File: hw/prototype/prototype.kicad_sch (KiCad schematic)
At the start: 0 parts

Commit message: More KiCAD files
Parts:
- added C1: C, symbol Device:C
- added D1: LED, LED_SMD:LED_Cree-XHP50_3V_HighDensity, symbol Device:LED
- added D2: D_Photo, OptoDevice:Kodenshi_LG206D, symbol Device:D_Photo
- added R1, R2: R_US, symbol Device:R_US
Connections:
- new net: D1.2 (A), R1.2
- new net GND: D1.1 (K), D2.2 (A)
- new net VCC: R1.1

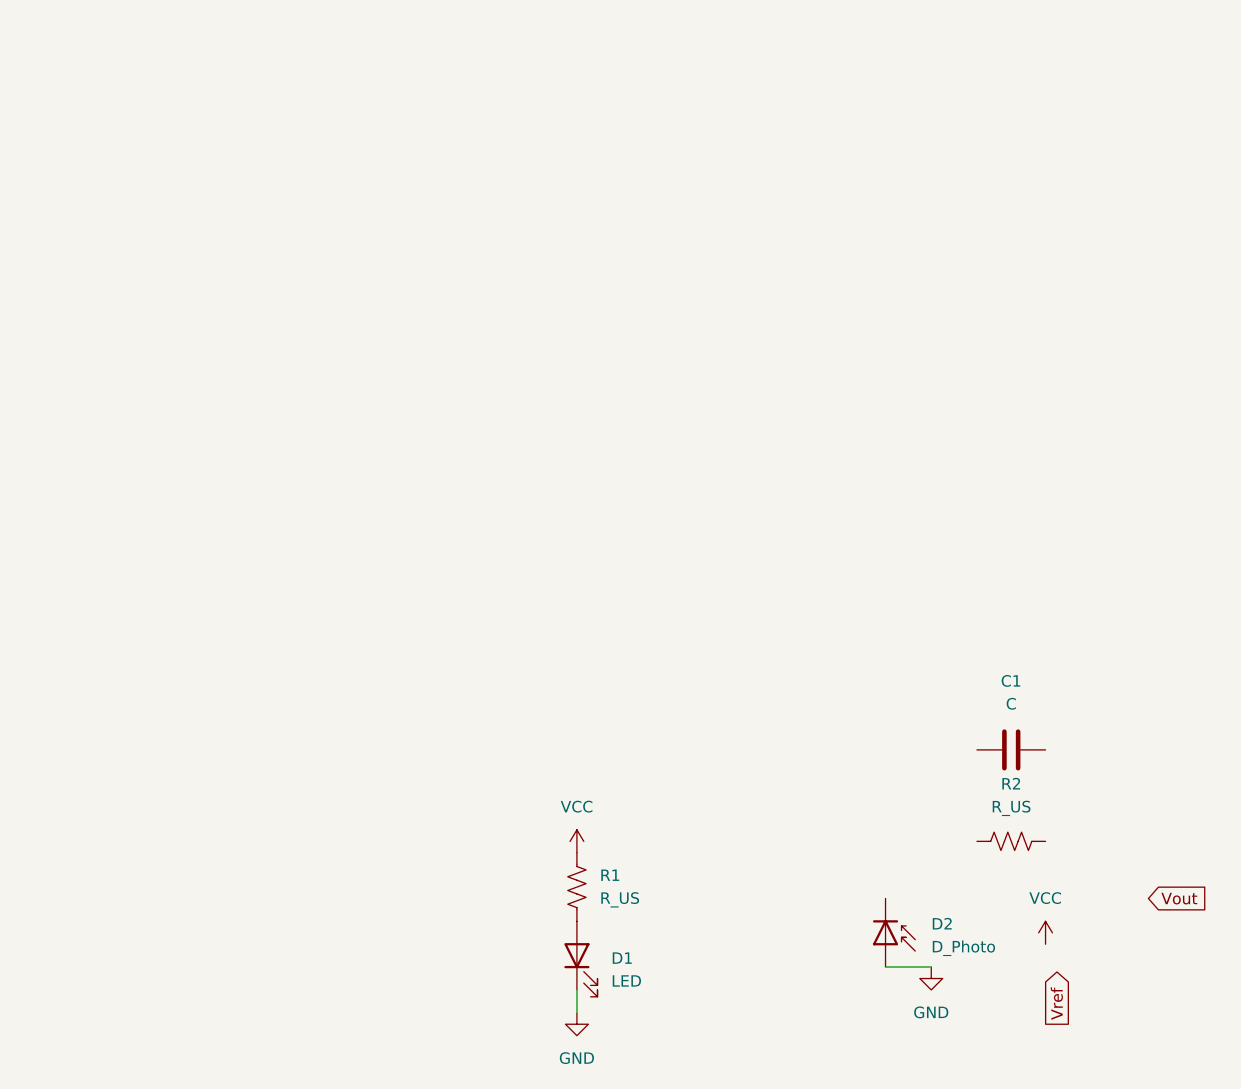
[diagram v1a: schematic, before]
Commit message: Added modified TI reference design
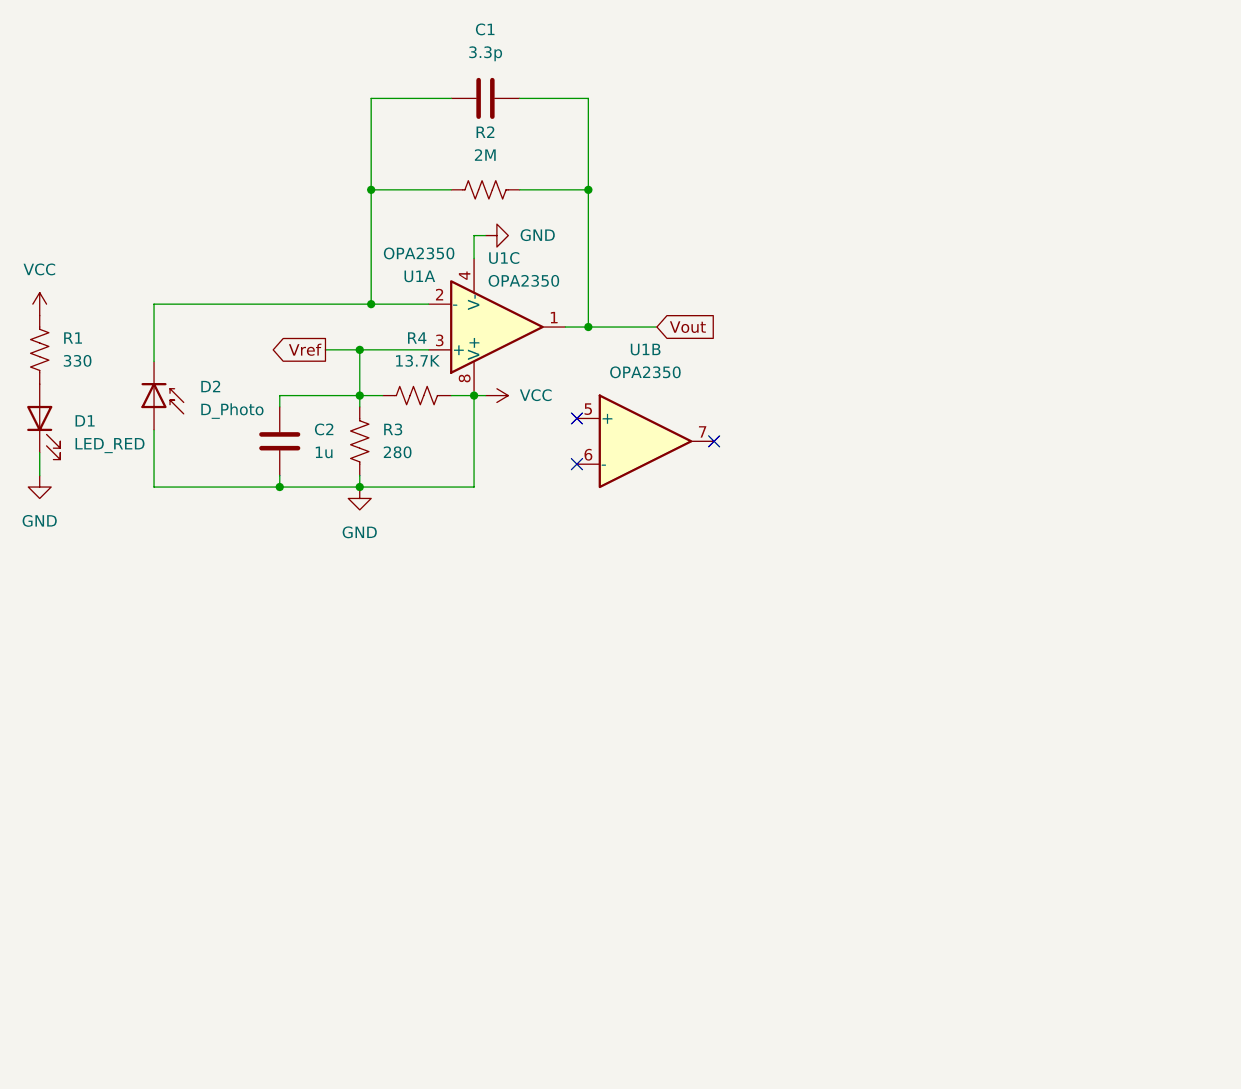
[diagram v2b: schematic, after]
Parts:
- added C2: 1u, symbol Device:C
- added R3: 280, symbol Device:R_US
- added R4: 13.7K, symbol Device:R_US
- added U1: OPA2350, ECE445L:DIP-8_W7.62mm_LongPads, symbol Project Library:OPA2350
- C1: value C -> 3.3p
- D1: value LED -> LED_RED
- R1: value R_US -> 330
- R2: value R_US -> 2M
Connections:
- net VCC is gone; now on net GND: R1.1
- net GND: now also C2.1, R3.1, R4.1, U1.4 (V-), U1.8 (V+)
- net Vout: now also C1.2, R2.2, U1.1
- net Vref: now also C2.2, R3.2, R4.2, U1.3 (+)
- net at C1.1: now also D2.1 (K), R2.1, U1.2 (-)
- no-connect marks 0 -> 3
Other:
- moved on the sheet: C1, D1, D2, R1, R2

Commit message: Finished schematic, basic FW
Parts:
- added R5: 10k, symbol Device:R_US
- added R6: 15k, symbol Device:R_US
- C1: value 3.3p -> 39pF
- R1: renamed from R2; value 2M -> 180K
- R2: renamed from R4; value 13.7K -> 50k
- R3: value 280 -> 1k
- renumbered R1 to R4
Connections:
- net GND: now also D2.1 (K), R6.2; no longer D2.2 (A)
- net Vout: now also R5.2, R6.1; no longer C1.2, R1.2, U1.1
- net Vref: now also U1.5 (+)
- net at U1.6 (-): now also U1.7
- net at C1.1, R1.1, U1.2 (-): now also D2.2 (A); no longer D2.1 (K)
- new net: C1.2, R1.2, R5.1, U1.1
- no-connect marks 3 -> 0
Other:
- note added: "- Full-scale output: 4.798V × 0.6 = 2.879V at ADC - Dark output: 0.1002V × 0.6 = 60.1mV at ADC - @4.95V, ADC sees 2.97V (under the 3.0V scale (safe))"
- note added: "Math for passive component values: 1. Select the gain resistor. R1 = (V_{oMax} − V_{oMin}) / I_{iMax} = (4.9V − 0.1V) / 27μA = 177.8kΩ ≈ 174kΩ (Standard Value) 2. Select the feedback capacitor to meet the circuit bandwidth. C1 ≤ 1 / (2π x R1 x f_{p}) C1 ≤ 1 / (2π x 174kΩ x 20kHz)) ≤ 45.7pF ≈ 39pF (C0G/NP0) (Standard Value) 3. Calculate the necessary op amp gain bandwidth (GBW) for the circuit to 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"
- moved on the sheet: D1, D2, R4, U1B

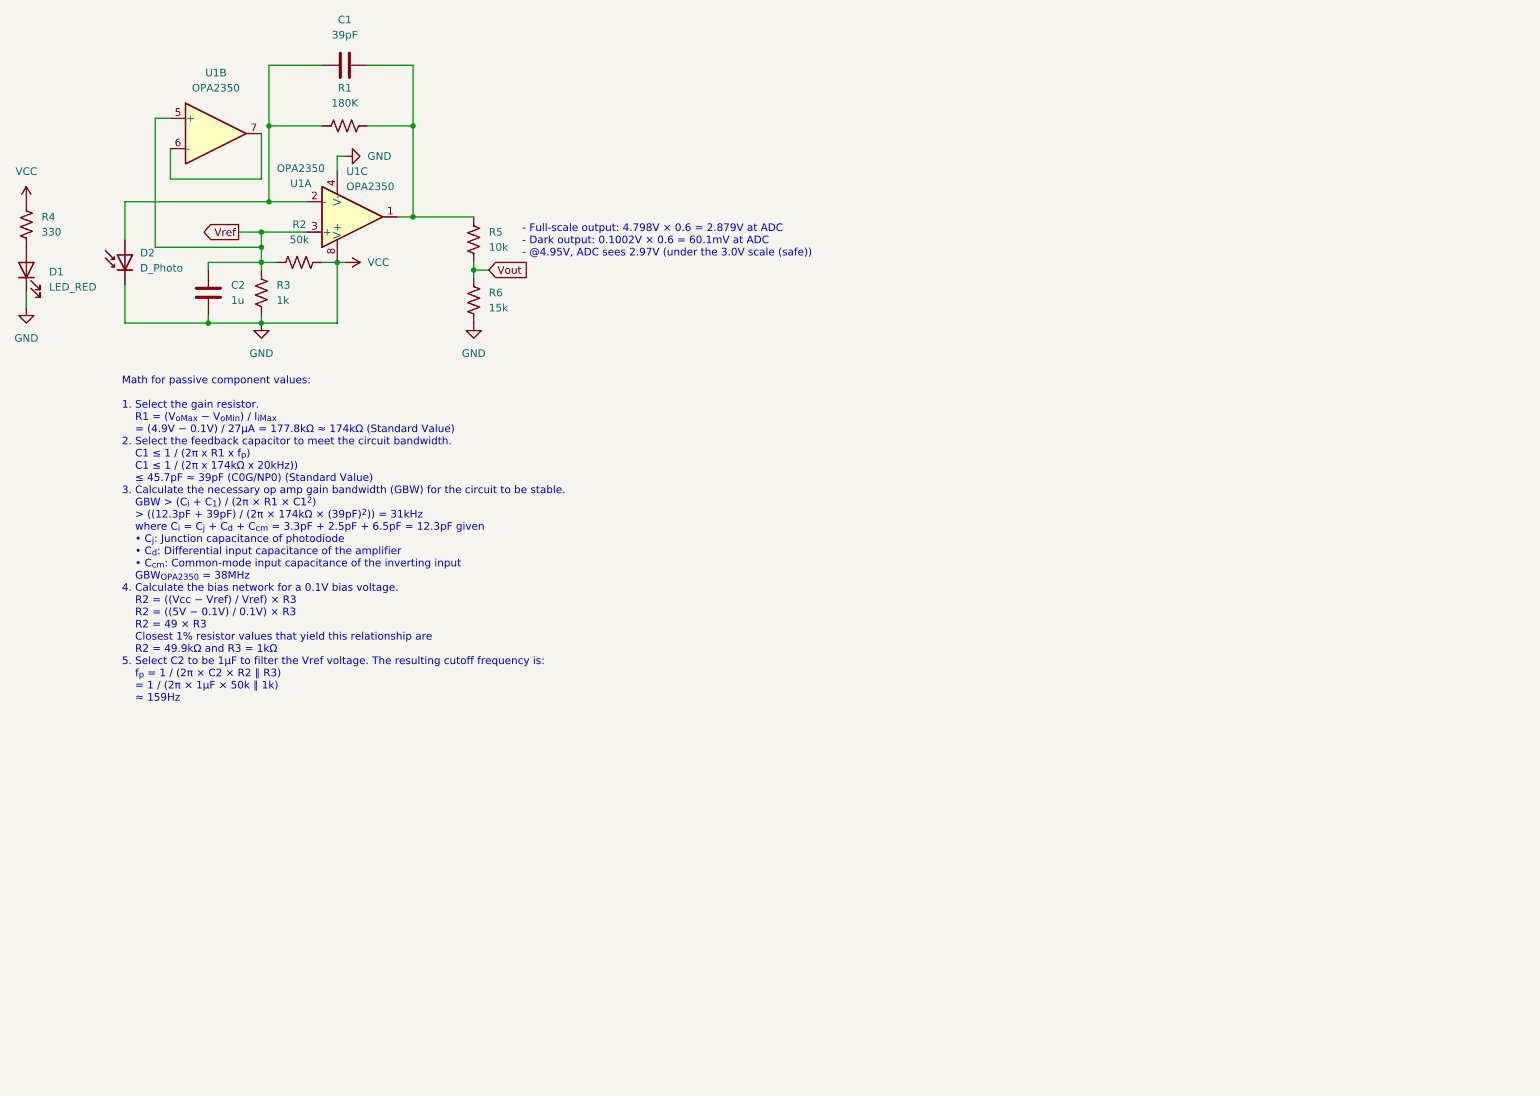
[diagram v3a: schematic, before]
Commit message: Started 3 diode design
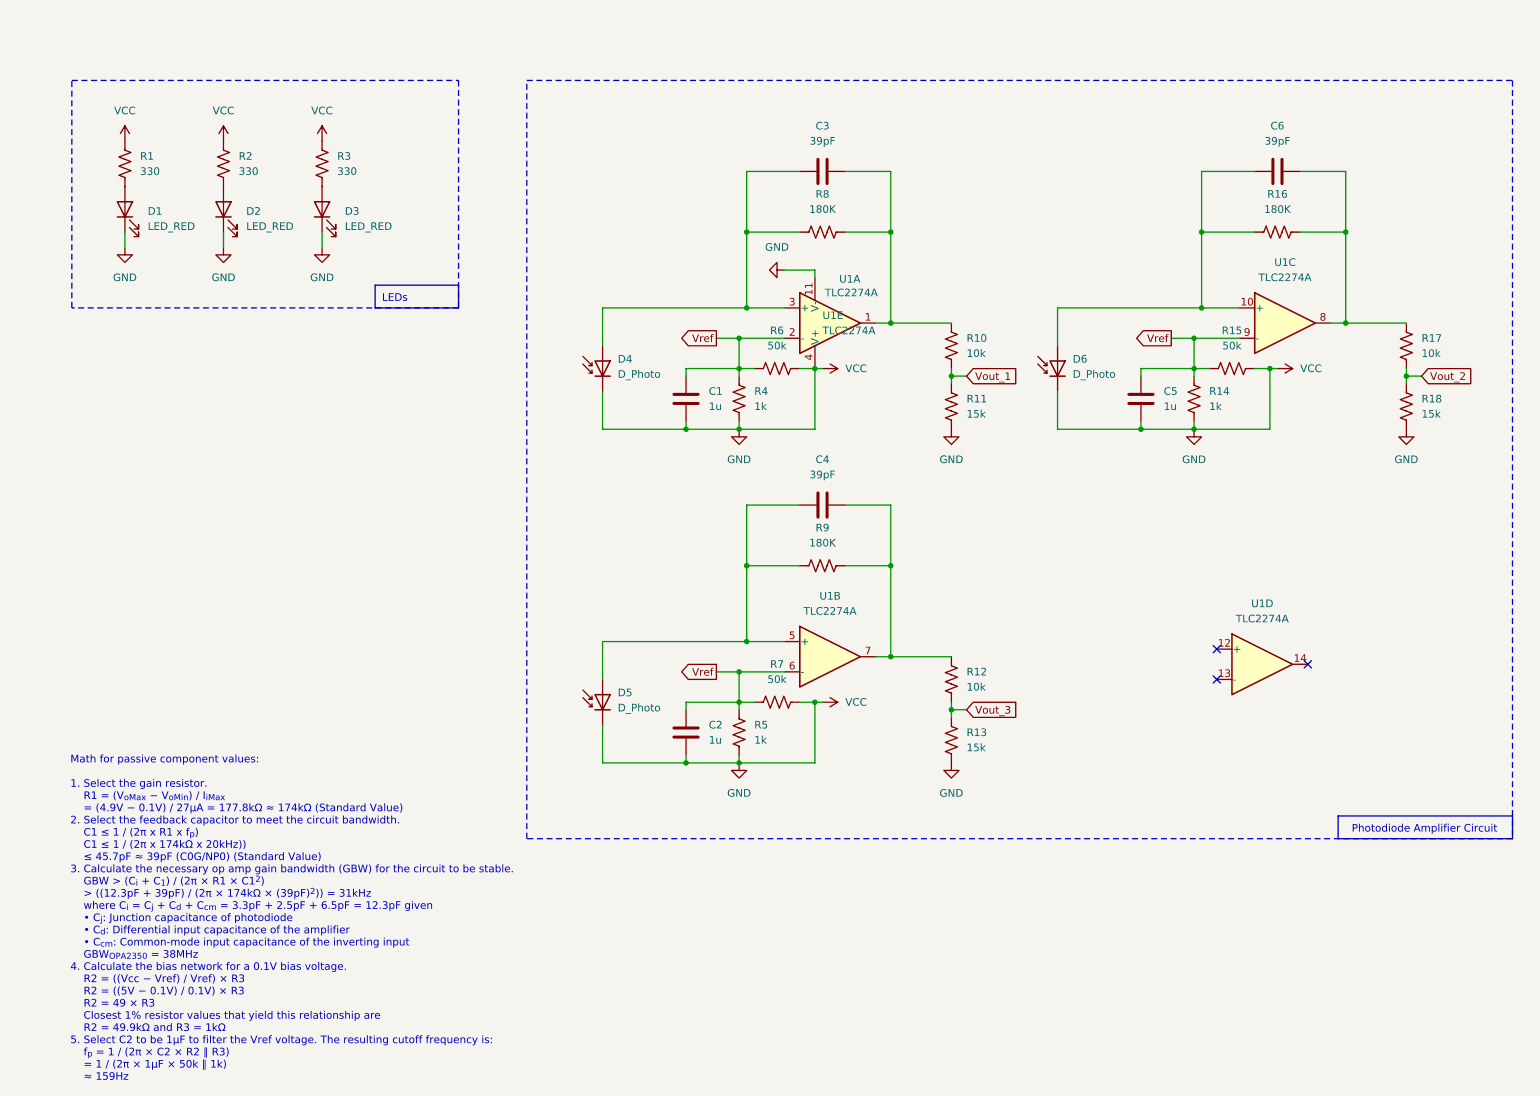
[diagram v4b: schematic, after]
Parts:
- removed U1: OPA2350, ECE445L:DIP-8_W7.62mm_LongPads, symbol Project Library:OPA2350
- added C2, C5: 1u, symbol Device:C
- added C4, C6: 39pF, symbol Device:C
- added D2, D3: LED_RED, LED_SMD:LED_Cree-XHP50_3V_HighDensity, symbol Device:LED
- added D5, D6: D_Photo, OptoDevice:Kodenshi_LG206D, symbol Device:D_Photo
- added R12, R17: 10k, symbol Device:R_US
- added R13, R18: 15k, symbol Device:R_US
- added R14, R5: 1k, symbol Device:R_US
- added R15, R7: 50k, symbol Device:R_US
- added R16, R9: 180K, symbol Device:R_US
- added R2, R3: 330, symbol Device:R_US
- added U1: TLC2274A, symbol Project Library:TLC2274A
- renumbered C2 to C1, C1 to C3, D2 to D4, R4 to R1, R5 to R10, R6 to R11, R3 to R4, R2 to R6, R1 to R8
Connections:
- net GND: now also C2.1, C5.1, D2.1 (K), D3.1 (K), D5.1 (K), D6.1 (K), R13.2, R14.1, R15.1, R18.2, R2.1, R3.1, R5.1, R7.1, U1.11 (V-), U1.4 (V+)
- net Vref: now also C2.2, C5.2, R14.2, R15.2, R5.2, R7.2, U1.2 (-), U1.6 (-), U1.9 (-)
- net at C3.2, R10.1, R8.2: now also U1.1
- net at C3.1, D4.2 (A), R8.1: now also U1.3 (+)
- net Vout renamed Vout_1
- new net: C4.1, D5.2 (A), R9.1, U1.5 (+)
- new net: C4.2, R12.1, R9.2, U1.7
- new net: C6.1, D6.2 (A), R16.1, U1.10 (+)
- new net: C6.2, R16.2, R17.1, U1.8
- new net: D3.2 (A), R3.2
- new net: D2.2 (A), R2.2
- new net Vout_2: R17.2, R18.1
- new net Vout_3: R12.2, R13.1
- no-connect marks 0 -> 3
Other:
- note added: "LEDs"
- note added: "Photodiode Amplifier Circuit"
- note removed: "- Full-scale output: 4.798V × 0.6 = 2.879V at ADC - Dark output: 0.1002V × 0.6 = 60.1mV at ADC - @4.95V, ADC sees 2.97V (under the 3.0V scale (safe))"
- moved on the sheet: C1, C3, D1, D4, R1, R10, R11, R4, R6, R8

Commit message: Finished 3 diode design
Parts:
- removed C2: 1u, symbol Device:C
- removed R14, R5: 1k, symbol Device:R_US
- removed R15, R7: 50k, symbol Device:R_US
- C5: value 1u -> 39pF
- renumbered C3 to C2, C4 to C3, C6 to C4, R12 to R10, R13 to R11, R16 to R12, R17 to R13, R18 to R14, R6 to R5, R8 to R6, R9 to R7, R10 to R8, R11 to R9
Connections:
- net GND: now also C5.2
- net Vout_1 renamed P0.28
- net Vout_2 renamed P0.04
- net Vout_3 renamed P0.03
- net Vref renamed P0.29
- net P0.29: no longer C5.2
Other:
- note added: "Outputs"
- moved on the sheet: U1D, U1E
